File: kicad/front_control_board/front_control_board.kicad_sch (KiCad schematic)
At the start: 70 parts, among them J1 MAIN_BOARD, J2 PROG, J3 DISPLAY, J4 LED_OUT, Q1 AO3400A, SW1 PEC11R-4215K-S00xx, SW2 BTN1, SW3 BTN4, SW4 BTN2, SW5 BTN3, U1 ESP32-WROOM-32UE

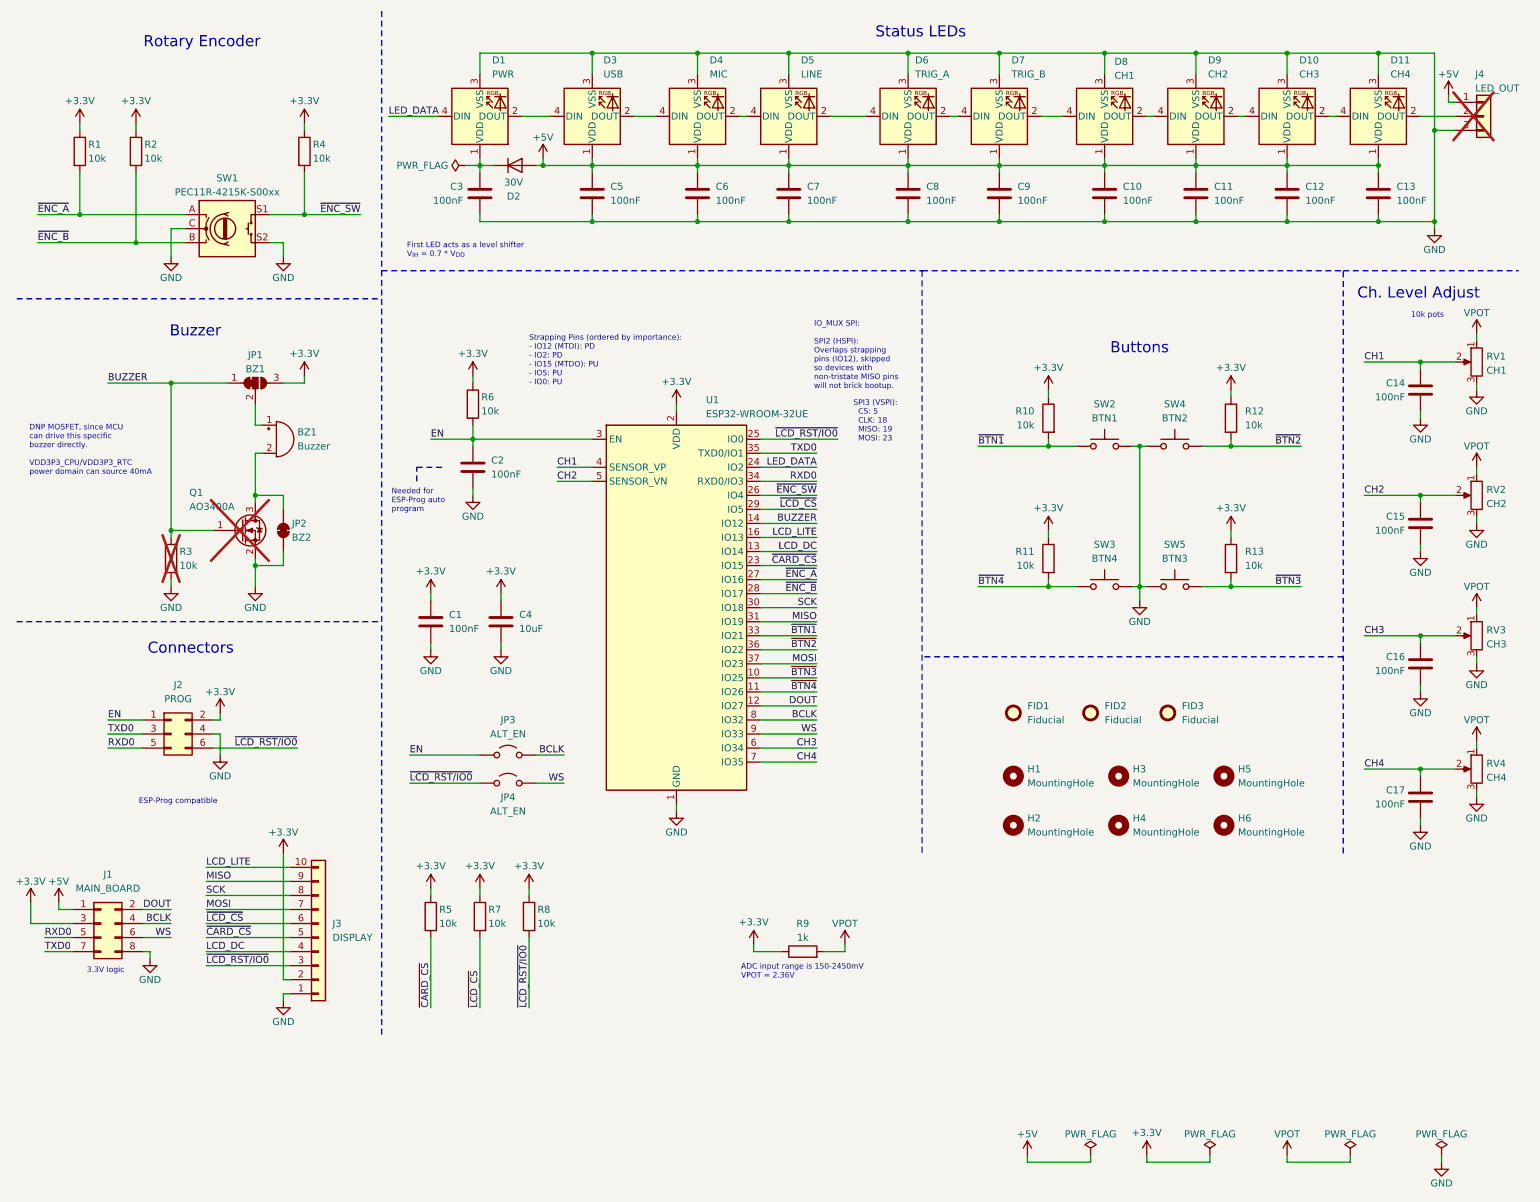
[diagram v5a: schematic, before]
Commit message: support flashing from main board
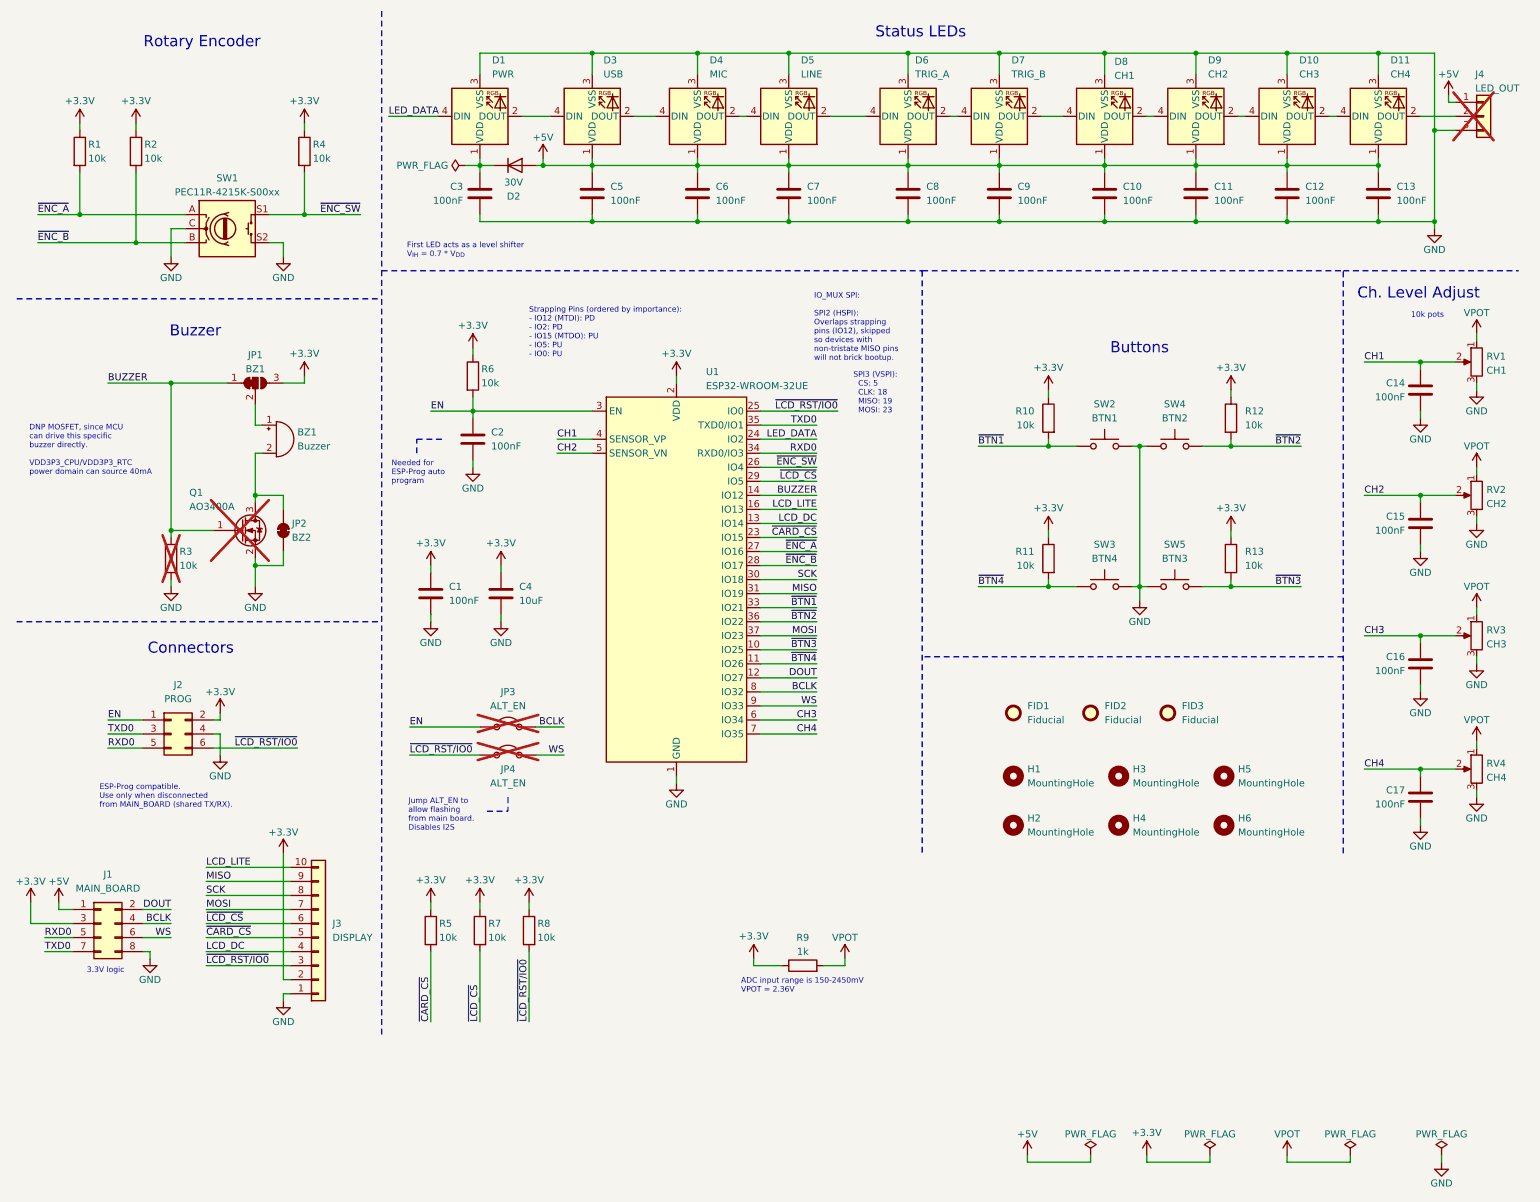
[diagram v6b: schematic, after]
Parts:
- JP3, JP4: footprint (none) -> Connector_PinHeader_2.54mm:PinHeader_1x02_P2.54mm_Vertical; LCSC (none) -> C492401; Service (none) -> HandAssembly; now not fitted
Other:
- note added: "ESP-Prog compatible. Use only when disconnected from MAIN_BOARD (shared TX/RX)."
- note added: "Jump ALT_EN to allow flashing from main board. Disables I2S"
- note removed: "ESP-Prog compatible"
- moved on the sheet: C1, C2, C4, R5, R6, R7, R8, R9, U1

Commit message: add draft front control board pcb
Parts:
- removed H5: MountingHole, MountingHole:MountingHole_2.2mm_M2, symbol Mechanical:MountingHole
- removed JP3, JP4: ALT_EN, Connector_PinHeader_2.54mm:PinHeader_1x02_P2.54mm_Vertical, symbol Jumper:Jumper_2_Open
- renumbered H6 to H5
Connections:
- net BCLK: now also U1.9 (IO33); no longer U1.8 (IO32)
- net DOUT: now also U1.10 (IO25); no longer U1.12 (IO27)
- net LCD_DC: now also U1.36 (IO22); no longer U1.13 (IO14)
- net WS: now also U1.8 (IO32); no longer U1.9 (IO33)
- net ~{BTN1}: now also U1.12 (IO27); no longer U1.33 (IO21)
- net ~{BTN2}: now also U1.11 (IO26); no longer U1.36 (IO22)
- net ~{BTN3}: now also U1.13 (IO14); no longer U1.10 (IO25)
- net ~{BTN4}: now also U1.33 (IO21); no longer U1.11 (IO26)
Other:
- note removed: "Jump ALT_EN to allow flashing from main board. Disables I2S"
- moved on the sheet: R5, R7, R8, R9

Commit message: cleanup
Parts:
- D4: value MIC -> LINE
- D5: value LINE -> MIC
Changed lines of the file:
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@@
 		(on_board yes)
 		(dnp no)
-		(fields_autoplaced yes)
 		(property "Reference" "D5"
-			(at 154.5941 21.59 0)
+			(at 154.686 21.844 0)
 			(effects
 				(font
@@
 			)
 		)
-		(property "Value" "LINE"
-			(at 154.5941 24.13 0)
+		(property "Value" "MIC"
+			(at 154.686 24.384 0)
 			(effects
 				(font
@@
 		(on_board yes)
 		(dnp no)
-		(fields_autoplaced yes)
 		(property "Reference" "D4"
-			(at 138.0841 21.59 0)
+			(at 136.906 21.844 0)
 			(effects
 				(font
@@
 			)
 		)
-		(property "Value" "MIC"
-			(at 138.0841 24.13 0)
-			(effects
-				(font
+		(property "Value" "LINE"
+			(at 136.906 24.384 0)
+			(effects
+				(font
